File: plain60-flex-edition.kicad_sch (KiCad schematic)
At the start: 173 parts, among them J1 HRO-TYPE-C-31-M-12, J2 ISP, J3 ai03_ud, K1 KEYSW, K10 KEYSW, K11 KEYSW, K12 KEYSW, K13 KEYSW, K14 KEYSW, K15 KEYSW, K15-1 KEYSW, K16 KEYSW, K17 KEYSW, K18 KEYSW, K19 KEYSW, K2 KEYSW, K20 KEYSW, K21 KEYSW, K22 KEYSW, K23 KEYSW, K24 KEYSW, K25 KEYSW, K26 KEYSW, K27 KEYSW, K28 KEYSW, K29 KEYSW, K3 KEYSW, K31 KEYSW, K31-1 KEYSW, K32 KEYSW, K33 KEYSW, K34 KEYSW, K35 KEYSW, K36 KEYSW, K37 KEYSW, K38 KEYSW, K39 KEYSW, K4 KEYSW, K40 KEYSW, K41 KEYSW, K42 KEYSW, K43 KEYSW, K44 KEYSW, K44-1 KEYSW, K46 KEYSW, K46-1 KEYSW, K47 KEYSW, K48 KEYSW, K49 KEYSW, K5 KEYSW, K50 KEYSW, K51 KEYSW, K52 KEYSW, K53 KEYSW, K54 KEYSW, K55 KEYSW, K56 KEYSW, K57 KEYSW, K58 KEYSW, K58-1 KEYSW, K59 KEYSW, K6 KEYSW, K61 KEYSW, K61-1 KEYSW, K62 KEYSW, K62-1 KEYSW, K63 KEYSW, K63-1 KEYSW, K67 KEYSW, K67-1 KEYSW, K7 KEYSW, K71 KEYSW, K72 KEYSW, K72-1 KEYSW, K73 KEYSW, K73-1 KEYSW, K74 KEYSW, K74-1 KEYSW, K8 KEYSW, K9 KEYSW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

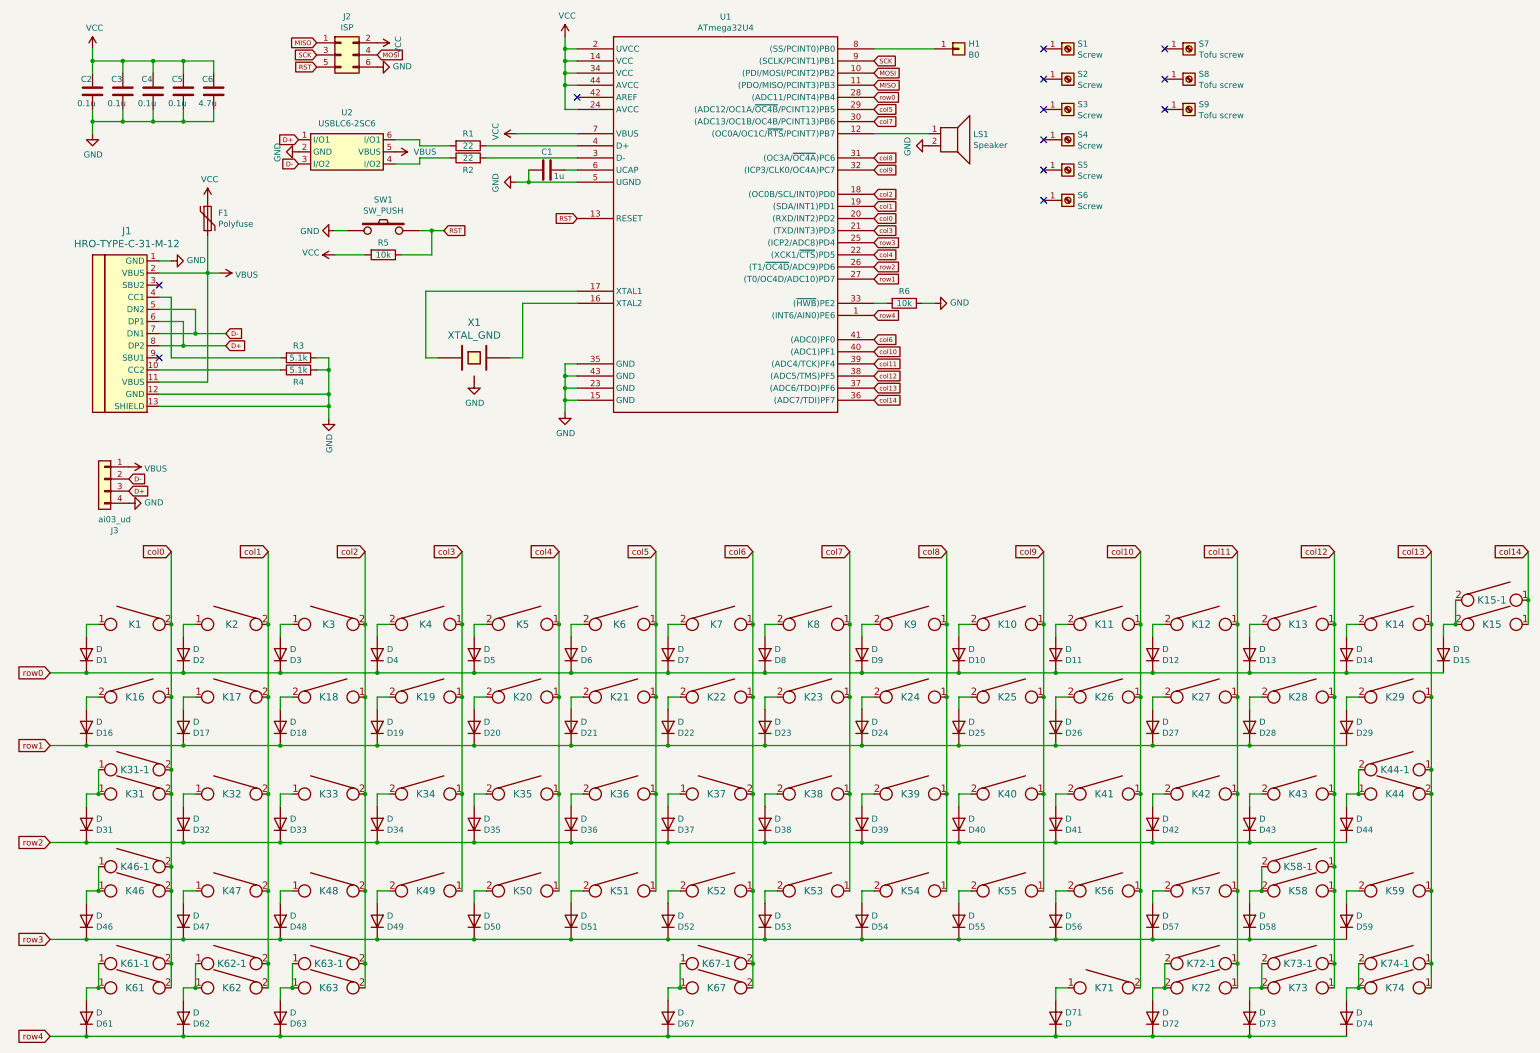
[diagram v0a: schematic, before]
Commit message: removed ansi and 6.25u support
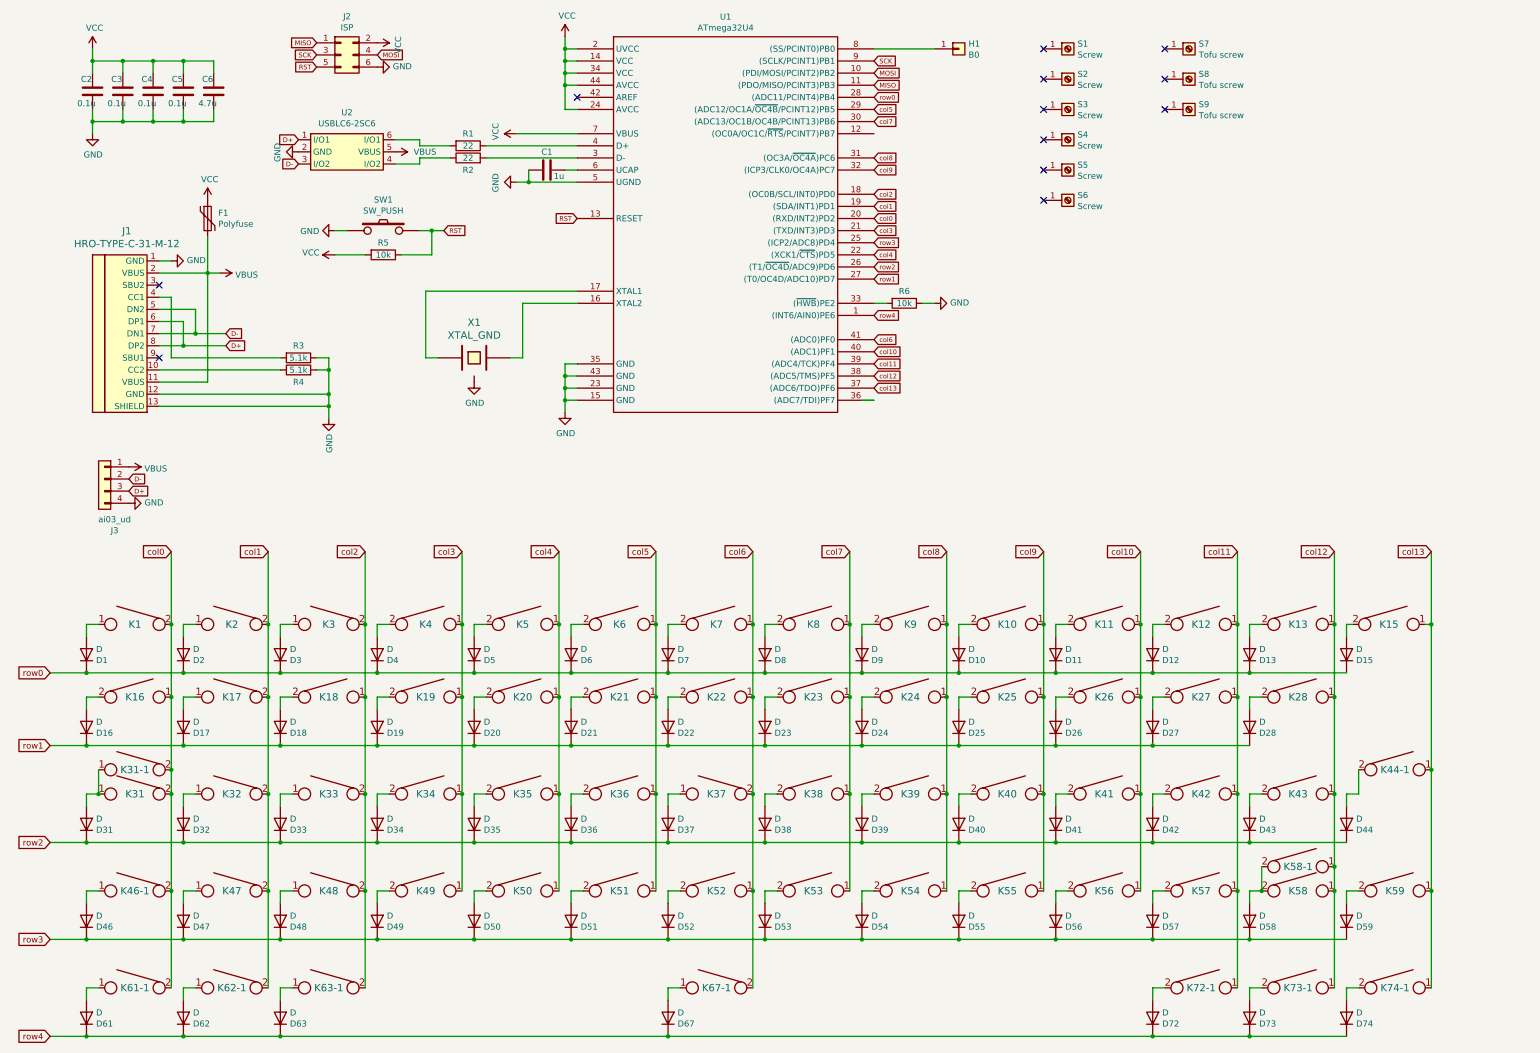
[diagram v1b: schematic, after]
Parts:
- removed D14, D29, D71: D, Keeb_components:D_0805, symbol Device:D
- removed K14, K15-1: KEYSW, Keeb_switches:CHERRY_PLATE_100H, symbol keyboard_parts:KEYSW
- removed K29: KEYSW, Keeb_switches:CHERRY_PLATE_150H, symbol keyboard_parts:KEYSW
- removed K44: KEYSW, Keeb_switches:CHERRY_PCB_225H_F, symbol keyboard_parts:KEYSW
- removed K46: KEYSW, Keeb_switches:CHERRY_PCB_225H, symbol keyboard_parts:KEYSW
- removed K61, K62, K63, K71, K72, K73, K74: KEYSW, Keeb_switches:CHERRY_PLATE_125H, symbol keyboard_parts:KEYSW
- removed K67: KEYSW, Keeb_switches:CHERRY_PCB_625H_F, symbol keyboard_parts:KEYSW
- removed LS1: Speaker, Keeb_components:speaker_AST1109MLTRQ, symbol Device:Speaker
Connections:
- net col13: now also K15.1
- net col14: no longer names the net of U1.36 ((ADC7/TDI)PF7)
- net col14: no longer K15.1
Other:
- moved on the sheet: D15, K15, K46-1, K61-1, K62-1, K63-1, K67-1, K72-1, K73-1, K74-1
